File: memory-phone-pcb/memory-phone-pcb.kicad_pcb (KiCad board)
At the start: 2 copper layers, 48.5 x 92 mm, 0 parts

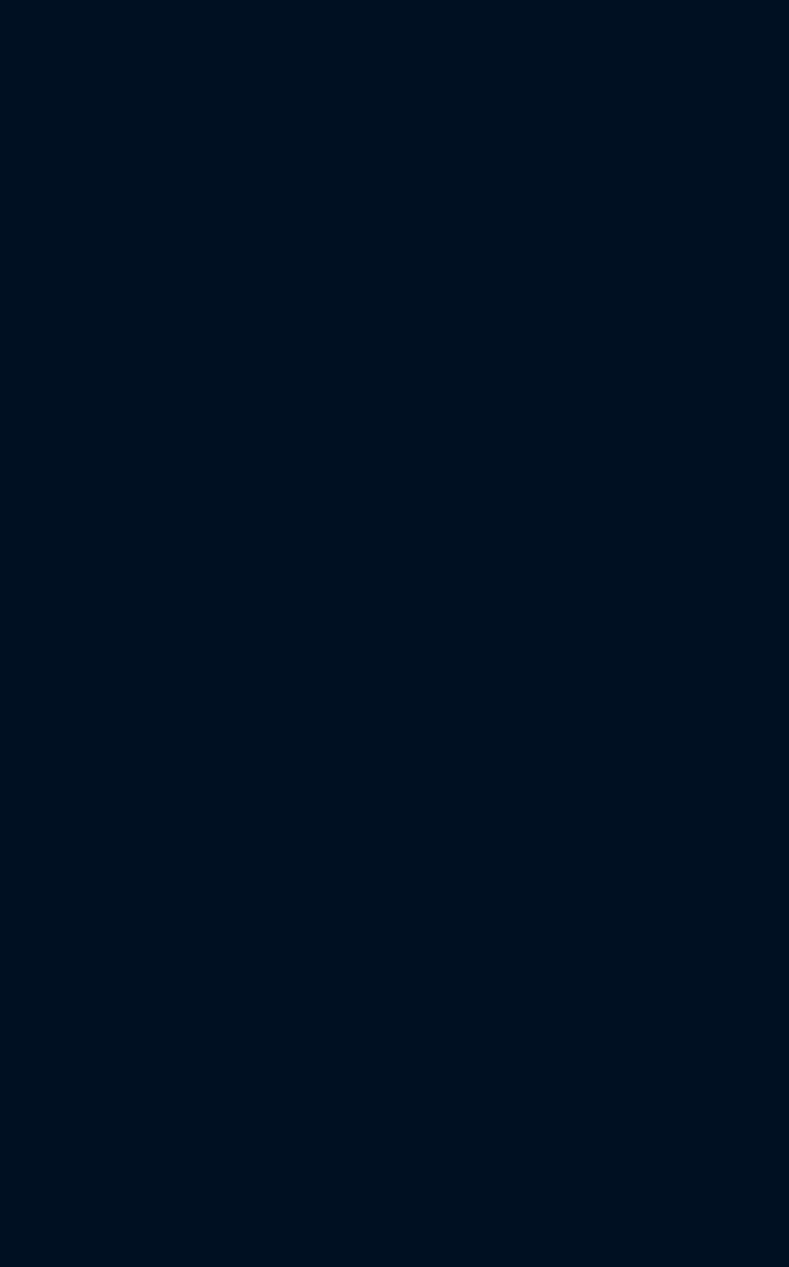
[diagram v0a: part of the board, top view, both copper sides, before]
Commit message: sch work adding rp2040
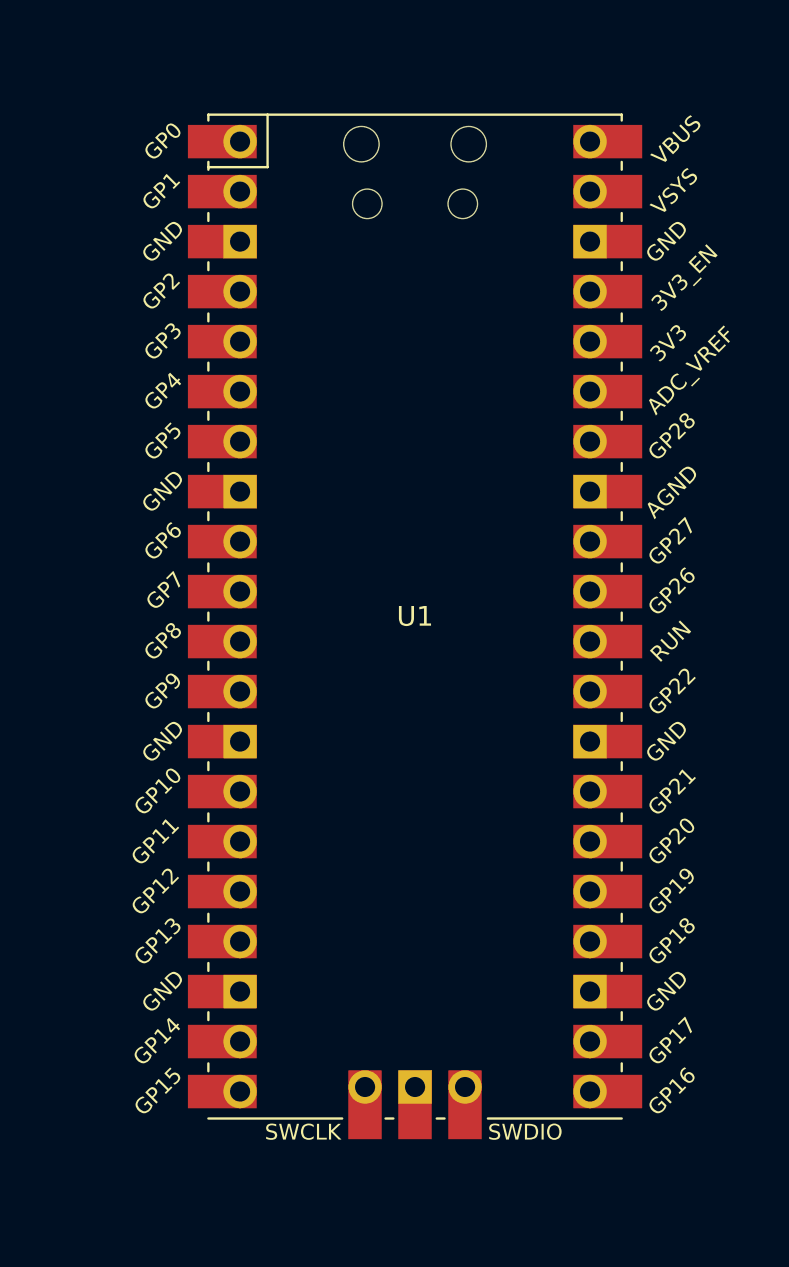
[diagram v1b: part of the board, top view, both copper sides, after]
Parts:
- added U1: Pico, MCU_RaspberryPi_and_Boards:RPi_Pico_SMD_TH, F.Cu at (113.6, 87.3)

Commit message: finished pcb
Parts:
- added C1: 10nF, Capacitor_SMD:C_0603_1608Metric_Pad1.08x0.95mm_HandSolder, F.Cu at (65.7, 68.3)
- added C2: 10nF, Capacitor_SMD:C_0603_1608Metric_Pad1.08x0.95mm_HandSolder, F.Cu at (65.7, 71.5)
- added C3: 0.1uF, Capacitor_SMD:C_0603_1608Metric_Pad1.08x0.95mm_HandSolder, F.Cu at (58.3, 134.3)
- added C4: 100nF, Capacitor_SMD:C_0603_1608Metric_Pad1.08x0.95mm_HandSolder, F.Cu at (69.1, 77.3)
- added C5: 100nF, Capacitor_SMD:C_0603_1608Metric_Pad1.08x0.95mm_HandSolder, F.Cu at (59.0, 67.2)
- added C6: 100nF, Capacitor_SMD:C_0603_1608Metric_Pad1.08x0.95mm_HandSolder, F.Cu at (49.5, 64.5)
- added C7: 10nF, Capacitor_SMD:C_0603_1608Metric_Pad1.08x0.95mm_HandSolder, F.Cu at (53.2, 67.1)
- added C8: 2.2uF, Capacitor_SMD:C_0603_1608Metric_Pad1.08x0.95mm_HandSolder, F.Cu at (56.3, 64.5)
- added J1: Conn_01x04, Connector_PinSocket_2.54mm:PinSocket_1x04_P2.54mm_Vertical, F.Cu at (71.1, 64.0)
- added J2: Conn_01x04, Connector_PinSocket_2.54mm:PinSocket_1x04_P2.54mm_Vertical, F.Cu at (76.3, 64.0)
- added J3: DM3D-SF, MemoryPhone_footprints:DM3D-SF, F.Cu at (58.1, 125.4)
- added R1: 22R, Resistor_SMD:R_0603_1608Metric_Pad0.98x0.95mm_HandSolder, F.Cu at (56.8, 134.3)
- added R2: 10kR, Resistor_SMD:R_0603_1608Metric_Pad0.98x0.95mm_HandSolder, F.Cu at (61.4, 134.3)
- added R3: 10kR, Resistor_SMD:R_0603_1608Metric_Pad0.98x0.95mm_HandSolder, F.Cu at (59.9, 134.3)
- added R4: 10kR, Resistor_SMD:R_0603_1608Metric_Pad0.98x0.95mm_HandSolder, F.Cu at (55.3, 134.3)
- added R5: 200R, Resistor_SMD:R_0603_1608Metric_Pad0.98x0.95mm_HandSolder, F.Cu at (65.7, 73.5)
- added R6: 10kR, Resistor_SMD:R_0603_1608Metric_Pad0.98x0.95mm_HandSolder, F.Cu at (53.8, 134.3)
- added R7: 1MR, Resistor_SMD:R_0603_1608Metric_Pad0.98x0.95mm_HandSolder, F.Cu at (57.0, 61.8)
- added R8: 10kR, Resistor_SMD:R_0603_1608Metric_Pad0.98x0.95mm_HandSolder, F.Cu at (80.0, 64.0)
- added R9: 10kR, Resistor_SMD:R_0603_1608Metric_Pad0.98x0.95mm_HandSolder, F.Cu at (80.0, 69.1)
- added RV1: TC33X-1-102E, MemoryPhone_footprints:TC33X-1, F.Cu at (65.2, 64.5)
- added U2: SN74AHCT1G125DBVR, Package_TO_SOT_SMD:SOT-23-5_HandSoldering, F.Cu at (65.7, 77.5)
- added U3: LP2985-1.5, Package_TO_SOT_SMD:SOT-23-5, F.Cu at (53.2, 64.5)
- added U4: Pico, MCU_RaspberryPi_and_Boards:RPi_Pico_SMD_TH, F.Cu at (95.8, 137.4)
- added U5: LM4040DBZ-3, Package_TO_SOT_SMD:SOT-23, F.Cu at (64.9, 143.4)
- U1: value Pico -> OPA196xDBV; footprint MCU_RaspberryPi_and_Boards:RPi_Pico_SMD_TH -> Package_TO_SOT_SMD:SOT-23-5
- moved U1 58.9 mm to (59.3, 64.6), turned to 180 degrees
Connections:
- U1 pad 1: unconnected-(U1-Pad1) -> /HANDSET_ADC_IN
- U1 pad 2: unconnected-(U1-Pad2) -> GND
- U1 pad 3: unconnected-(U1-Pad3) -> /HANDSET_MIC_IN
- U1 pad 4: unconnected-(U1-Pad4) -> /HANDSET_ADC_IN
- U1 pad 5: unconnected-(U1-Pad5) -> +3V3
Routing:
- net /HANDSET_ADC_IN: track 0.00 -> 117.1 mm, vias 0 -> 2
- net /HANDSET_PWM_OUT: track 0.00 -> 105.1 mm
- net /HANG_UP: track 0.00 -> 100.2 mm
- net /DIAL: track 0.00 -> 98.3 mm
- net +3V3: track 0.00 -> 64.4 mm, vias 0 -> 5
- net /ADC_VREF: track 0.00 -> 47.2 mm
- net /SD_SCK: track 0.00 -> 38.1 mm, vias 0 -> 2
- net /SD_SDI: track 0.00 -> 38.1 mm, vias 0 -> 2
- net /SD_SDO: track 0.00 -> 33.2 mm, vias 0 -> 2
- net /SD_CSn: track 0.00 -> 28.3 mm
- net GND: track 0.00 -> 25.0 mm, vias 0 -> 17
- net /HANDSET_MIC_IN: track 0.00 -> 13.7 mm
- net Net-(R5-Pad2): track 0.00 -> 13.6 mm
- net Net-(C1-Pad1): track 0.00 -> 7.70 mm
- net Net-(C2-Pad1): track 0.00 -> 5.66 mm
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- added copper zone on F.Cu, net +3V3
- added copper zone on B.Cu, net GND
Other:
- board size 48.5 x 92 mm -> 74.5 x 92.7 mm
